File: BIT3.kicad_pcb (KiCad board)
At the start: 2 copper layers, 121.3 x 109.4 mm, 49 parts, among them J1 Conn_02x04_Odd_Even, J2 Conn_01x02_Pin, J3 Conn_01x04_Socket, J4 Conn_02x02_Odd_Even, Q1 2SC1815, SW1 SW_SPDT, SW2 SW_Push, SW3 SW_Push, U2 FODM217A, U3 FODM217A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

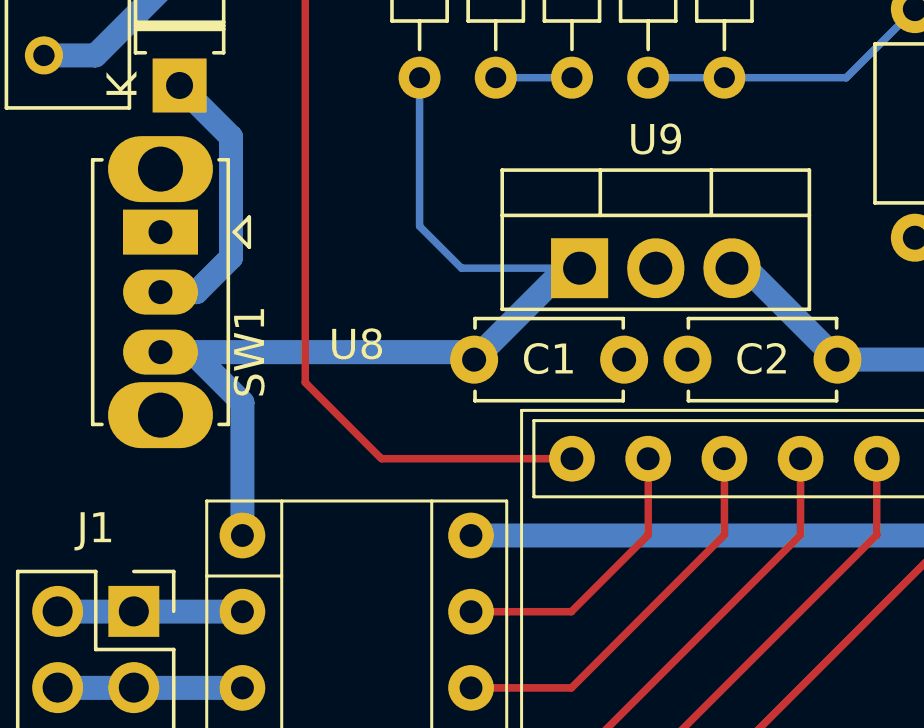
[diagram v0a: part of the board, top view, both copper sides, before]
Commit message: モータの電源を BATT から 5V に変更
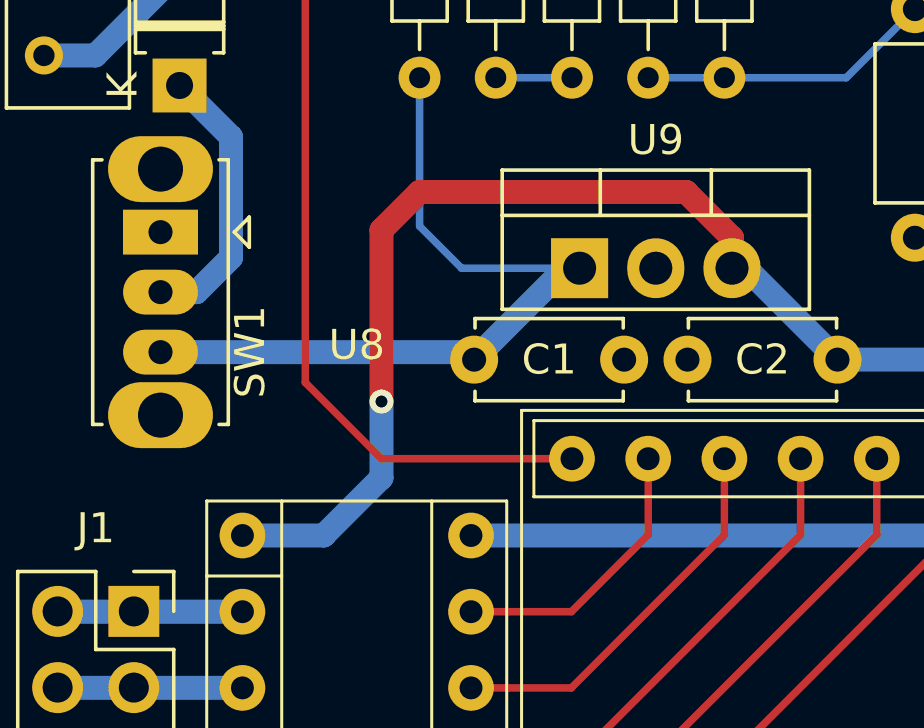
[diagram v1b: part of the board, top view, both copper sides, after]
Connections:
- U8 pad 1: /V_Battery -> +5V
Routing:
- net +5V: track 52.9 -> 80.5 mm, vias 3 -> 4
- net /V_Battery: track 34.1 -> 27.2 mm
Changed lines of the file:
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@@
       (stroke (width 0.1) (type default)) (layer "F.SilkS"))
     (pad "1" thru_hole circle (at -3.81 -6.35) (size 1.524 1.524) (drill 0.762) (layers "*.Cu" "*.Mask")
-      (net 64 "/V_Battery") (pinfunction "VM") (pintype "power_in"))
+      (net 14 "+5V") (pinfunction "VM") (pintype "power_in"))
     (pad "2" thru_hole circle (at -3.81 -3.81) (size 1.524 1.524) (drill 0.762) (layers "*.Cu" "*.Mask")
       (net 37 "Net-(J1-Pin_1)") (pinfunction "AOUT1") (pintype "output"))
@@
   (segment (start 190.5 76.835) (end 220.5 76.835) (width 0.25) (layer "F.Cu") (net 13))
   (segment (start 161.29 78.486) (end 161.29 80.264) (width 0.25) (layer "F.Cu") (net 13))
+  (segment (start 125.73 87.63) (end 125.73 93.345) (width 0.8) (layer "F.Cu") (net 14))
+  (segment (start 127 86.36) (end 125.73 87.63) (width 0.8) (layer "F.Cu") (net 14))
   (segment (start 171.704 91.948) (end 172.72 92.964) (width 0.8) (layer "F.Cu") (net 14))
   (segment (start 158.496 91.948) (end 171.704 91.948) (width 0.8) (layer "F.Cu") (net 14))
+  (segment (start 137.414 87.884) (end 135.89 86.36) (width 0.8) (layer "F.Cu") (net 14))
+  (segment (start 135.89 86.36) (end 127 86.36) (width 0.8) (layer "F.Cu") (net 14))
+  (segment (start 137.414 88.9) (end 137.414 87.884) (width 0.8) (layer "F.Cu") (net 14))
   (segment (start 172.72 92.964) (end 172.72 95.25) (width 0.8) (layer "F.Cu") (net 14))
   (via (at 160.02 91.948) (size 0.8) (drill 0.4) (layers "F.Cu" "B.Cu") (net 14))
   (via (at 158.496 91.948) (size 0.8) (drill 0.4) (layers "F.Cu" "B.Cu") (net 14))
   (via (at 159.258 91.948) (size 0.8) (drill 0.4) (layers "F.Cu" "B.Cu") (net 14))
+  (via (at 125.73 93.345) (size 0.8) (drill 0.4) (layers "F.Cu" "B.Cu") (net 14))
+  (segment (start 123.805 97.81) (end 121.095 97.81) (width 0.8) (layer "B.Cu") (net 14))
   (segment (start 177.165 97.155) (end 177.165 100.33) (width 0.8) (layer "B.Cu") (net 14))
   (segment (start 158.496 91.948) (end 159.258 91.948) (width 0.8) (layer "B.Cu") (net 14))
@@
   (segment (start 140.93 91.948) (end 158.496 91.948) (width 0.8) (layer "B.Cu") (net 14))
   (segment (start 177.165 100.33) (end 178.435 101.6) (width 0.8) (layer "B.Cu") (net 14))
+  (segment (start 125.73 93.345) (end 125.73 95.885) (width 0.8) (layer "B.Cu") (net 14))
+  (segment (start 125.73 95.885) (end 123.805 97.81) (width 0.8) (layer "B.Cu") (net 14))
   (segment (start 159.258 91.948) (end 160.02 91.948) (width 0.8) (layer "B.Cu") (net 14))
   (segment (start 191.77 58.27) (end 188.5 55) (width 0.25) (layer "F.Cu") (net 15))
@@
   (segment (start 119.414 91.698) (end 118.364 91.698) (width 0.8) (layer "B.Cu") (net 64))
   (segment (start 131.866 88.9) (end 128.818 91.948) (width 0.8) (layer "B.Cu") (net 64))
-  (segment (start 121.095 93.379) (end 119.414 91.698) (width 0.8) (layer "B.Cu") (net 64))
   (segment (start 128.568 91.698) (end 128.818 91.948) (width 0.8) (layer "B.Cu") (net 64))
-  (segment (start 121.095 97.81) (end 121.095 93.379) (width 0.8) (layer "B.Cu") (net 64))
   (segment (start 165.1 106.68) (end 180.34 106.68) (width 0.25) (layer "B.Cu") (net 65))
   (segment (start 151.13 104.14) (end 144.78 110.49) (width 0.25) (layer "B.Cu") (net 66))

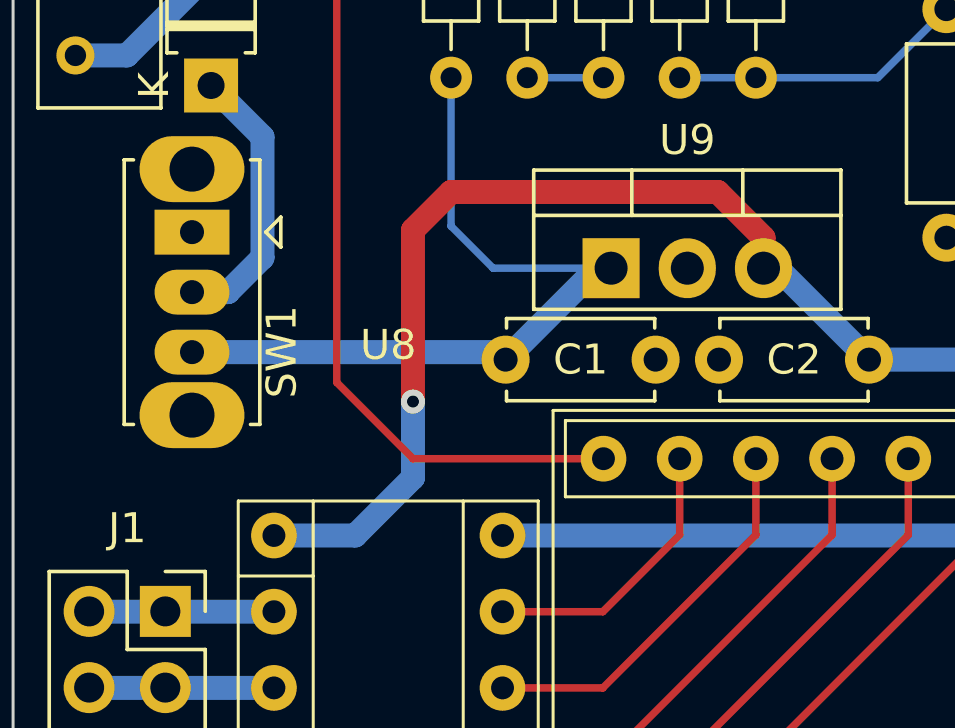
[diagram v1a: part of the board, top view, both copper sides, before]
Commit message: モータ電源を BATT に戻した
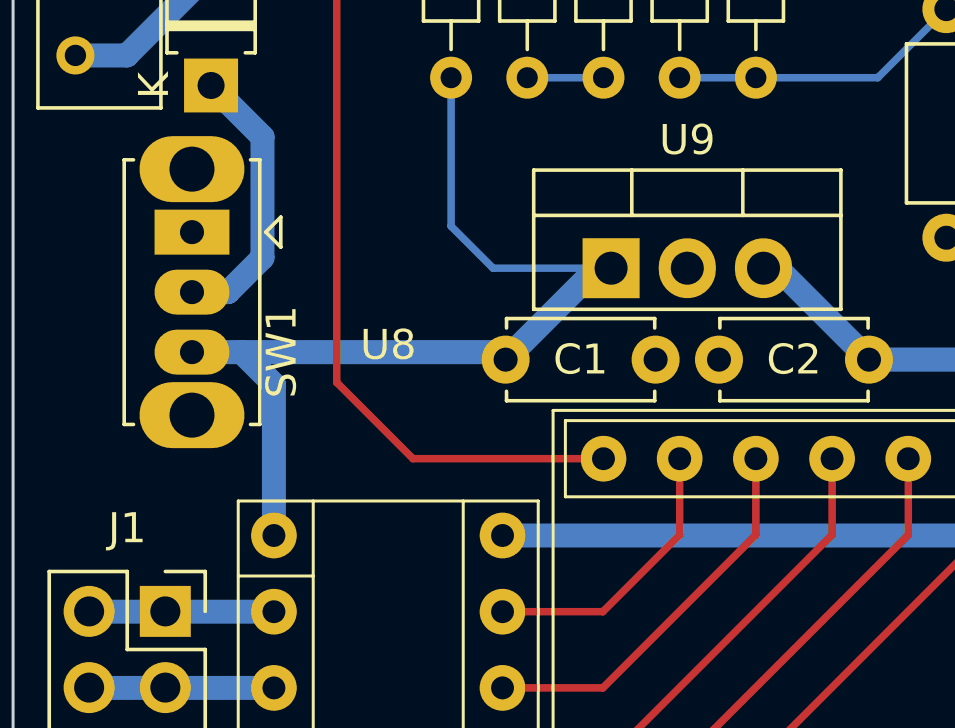
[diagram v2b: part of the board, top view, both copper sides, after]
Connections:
- U8 pad 1: +5V -> /V_Battery
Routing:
- net +5V: track 80.5 -> 52.9 mm, vias 4 -> 3
- net /V_Battery: track 27.2 -> 32.8 mm
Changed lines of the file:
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@@
       (stroke (width 0.1) (type default)) (layer "F.SilkS"))
     (pad "1" thru_hole circle (at -3.81 -6.35) (size 1.524 1.524) (drill 0.762) (layers "*.Cu" "*.Mask")
-      (net 14 "+5V") (pinfunction "VM") (pintype "power_in"))
+      (net 64 "/V_Battery") (pinfunction "VM") (pintype "power_in"))
     (pad "2" thru_hole circle (at -3.81 -3.81) (size 1.524 1.524) (drill 0.762) (layers "*.Cu" "*.Mask")
       (net 37 "Net-(J1-Pin_1)") (pinfunction "AOUT1") (pintype "output"))
@@
   (segment (start 190.5 76.835) (end 220.5 76.835) (width 0.25) (layer "F.Cu") (net 13))
   (segment (start 161.29 78.486) (end 161.29 80.264) (width 0.25) (layer "F.Cu") (net 13))
-  (segment (start 125.73 87.63) (end 125.73 93.345) (width 0.8) (layer "F.Cu") (net 14))
-  (segment (start 127 86.36) (end 125.73 87.63) (width 0.8) (layer "F.Cu") (net 14))
   (segment (start 171.704 91.948) (end 172.72 92.964) (width 0.8) (layer "F.Cu") (net 14))
   (segment (start 158.496 91.948) (end 171.704 91.948) (width 0.8) (layer "F.Cu") (net 14))
-  (segment (start 137.414 87.884) (end 135.89 86.36) (width 0.8) (layer "F.Cu") (net 14))
-  (segment (start 135.89 86.36) (end 127 86.36) (width 0.8) (layer "F.Cu") (net 14))
-  (segment (start 137.414 88.9) (end 137.414 87.884) (width 0.8) (layer "F.Cu") (net 14))
   (segment (start 172.72 92.964) (end 172.72 95.25) (width 0.8) (layer "F.Cu") (net 14))
   (via (at 160.02 91.948) (size 0.8) (drill 0.4) (layers "F.Cu" "B.Cu") (net 14))
   (via (at 158.496 91.948) (size 0.8) (drill 0.4) (layers "F.Cu" "B.Cu") (net 14))
   (via (at 159.258 91.948) (size 0.8) (drill 0.4) (layers "F.Cu" "B.Cu") (net 14))
-  (via (at 125.73 93.345) (size 0.8) (drill 0.4) (layers "F.Cu" "B.Cu") (net 14))
-  (segment (start 123.805 97.81) (end 121.095 97.81) (width 0.8) (layer "B.Cu") (net 14))
   (segment (start 177.165 97.155) (end 177.165 100.33) (width 0.8) (layer "B.Cu") (net 14))
   (segment (start 158.496 91.948) (end 159.258 91.948) (width 0.8) (layer "B.Cu") (net 14))
@@
   (segment (start 140.93 91.948) (end 158.496 91.948) (width 0.8) (layer "B.Cu") (net 14))
   (segment (start 177.165 100.33) (end 178.435 101.6) (width 0.8) (layer "B.Cu") (net 14))
-  (segment (start 125.73 93.345) (end 125.73 95.885) (width 0.8) (layer "B.Cu") (net 14))
-  (segment (start 125.73 95.885) (end 123.805 97.81) (width 0.8) (layer "B.Cu") (net 14))
   (segment (start 159.258 91.948) (end 160.02 91.948) (width 0.8) (layer "B.Cu") (net 14))
   (segment (start 191.77 58.27) (end 188.5 55) (width 0.25) (layer "F.Cu") (net 15))
@@
   (segment (start 127 87.5) (end 128.4 88.9) (width 0.25) (layer "B.Cu") (net 64))
   (segment (start 132.334 88.9) (end 131.866 88.9) (width 0.8) (layer "B.Cu") (net 64))
+  (segment (start 120.015 91.698) (end 128.568 91.698) (width 0.8) (layer "B.Cu") (net 64))
   (segment (start 127 82.55) (end 127 87.5) (width 0.25) (layer "B.Cu") (net 64))
-  (segment (start 118.364 91.698) (end 128.568 91.698) (width 0.8) (layer "B.Cu") (net 64))
   (segment (start 128.4 88.9) (end 132.334 88.9) (width 0.25) (layer "B.Cu") (net 64))
-  (segment (start 119.414 91.698) (end 118.364 91.698) (width 0.8) (layer "B.Cu") (net 64))
+  (segment (start 118.364 91.698) (end 120.015 91.698) (width 0.8) (layer "B.Cu") (net 64))
+  (segment (start 120.015 91.698) (end 121.095 92.778) (width 0.8) (layer "B.Cu") (net 64))
   (segment (start 131.866 88.9) (end 128.818 91.948) (width 0.8) (layer "B.Cu") (net 64))
+  (segment (start 121.095 92.778) (end 121.095 97.81) (width 0.8) (layer "B.Cu") (net 64))
   (segment (start 128.568 91.698) (end 128.818 91.948) (width 0.8) (layer "B.Cu") (net 64))
   (segment (start 165.1 106.68) (end 180.34 106.68) (width 0.25) (layer "B.Cu") (net 65))

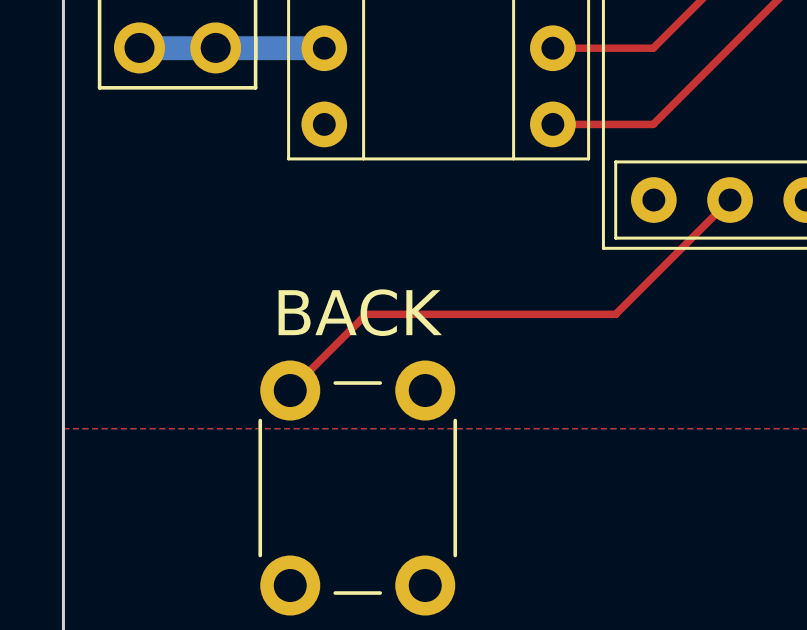
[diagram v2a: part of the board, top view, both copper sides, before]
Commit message: BACK -> EXEC
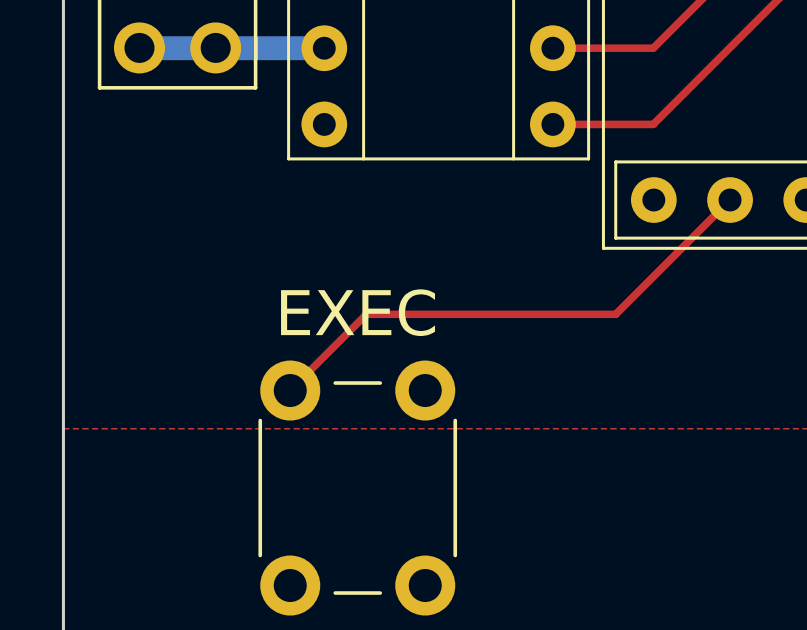
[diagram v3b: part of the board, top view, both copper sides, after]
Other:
- board text added: "EXEC"
- board text removed: "BACK"
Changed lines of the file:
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@@
     )
   )
-  (gr_text "BACK" (at 122.174 116.84) (layer "F.SilkS")
+  (gr_text "EXEC" (at 122.174 116.84) (layer "F.SilkS")
     (effects (font (size 1.5 1.5) (thickness 0.2)))
   )

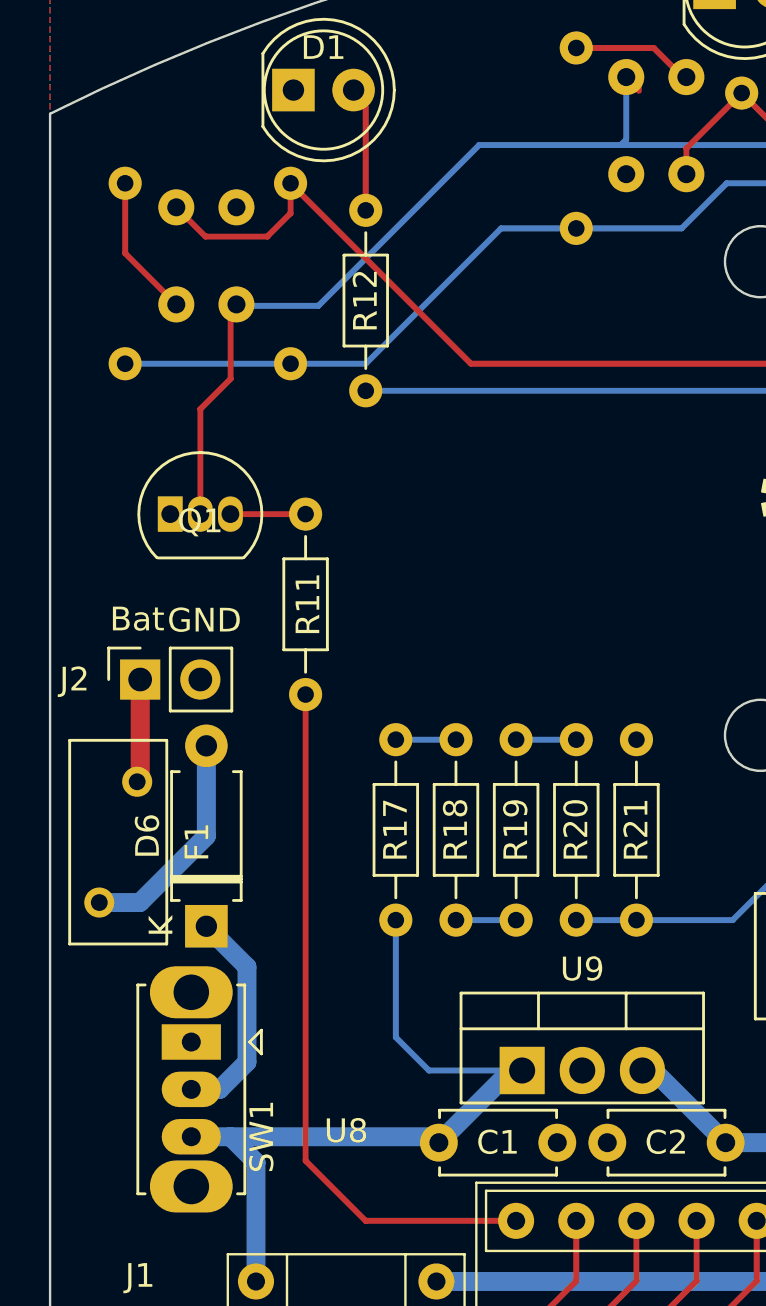
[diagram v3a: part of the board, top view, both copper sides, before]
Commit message: 赤外線 LED 用トランジスタを変更
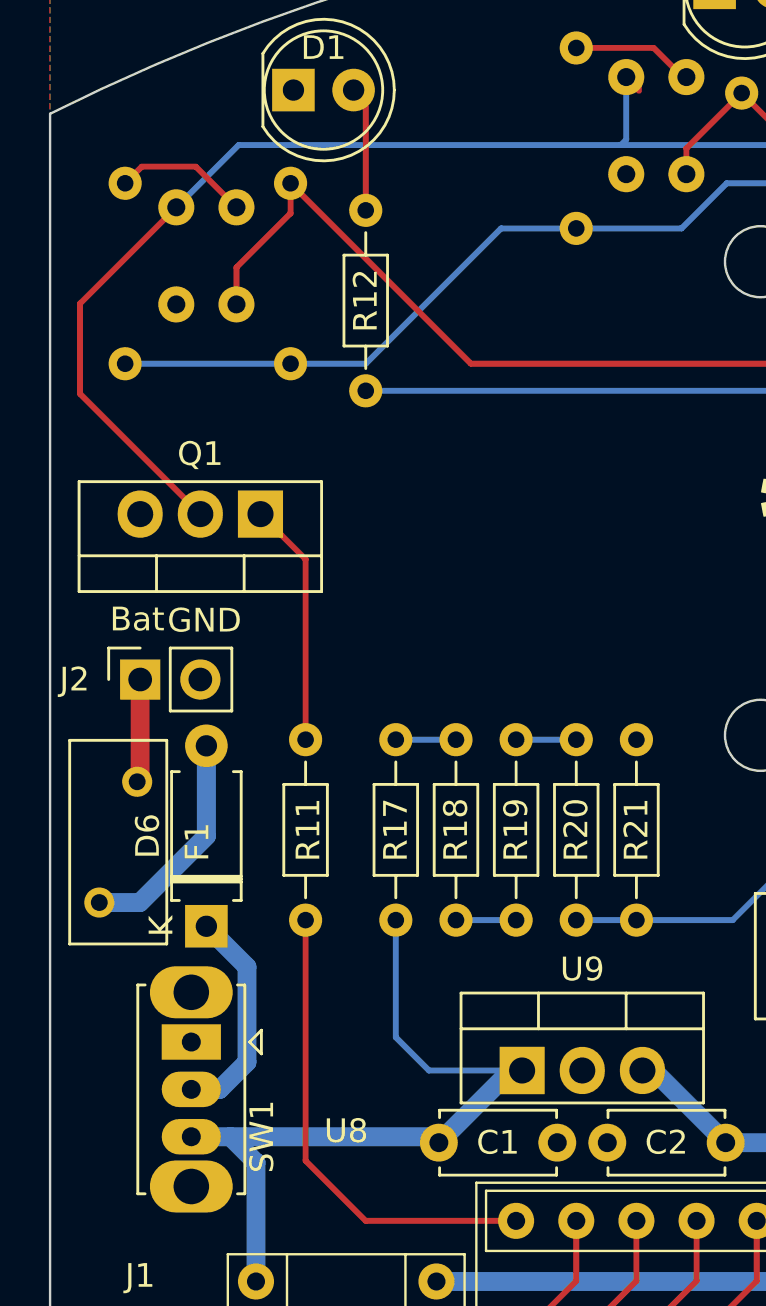
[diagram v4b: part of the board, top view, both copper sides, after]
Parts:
- Q1: value 2SC1815 -> BSP89; footprint Package_TO_SOT_THT:TO-92_Inline -> Package_TO_SOT_THT:TO-220-3_Vertical
- moved R11 9.52 mm to (123.2, 82.5)
- moved Q1 3.81 mm to (121.3, 65.4), turned to 180 degrees
- turned U2 to 180 degrees
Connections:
- Q1 pad 1: GND -> Net-(Q1-G)
- Q1 pad 3: Net-(Q1-B) -> GND
- R11 pad 2: Net-(Q1-B) -> Net-(Q1-G)
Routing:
- net Net-(Q1-G): track 0.00 -> 10.3 mm
- net /FET_B: track 29.6 -> 20.1 mm
- net /FET_D: track 145.7 -> 153.6 mm
- net Net-(Q1-B): track 3.17 -> 0.00 mm
- net /sensor_L: track 56.2 -> 55.6 mm

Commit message: Tr 置き換え，部品表更新
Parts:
- moved R11 5.72 mm to (123.2, 76.8)
- moved Q1 1.91 mm to (121.3, 63.5)
- turned U2 to 0 degrees
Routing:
- net /FET_D: track 153.6 -> 143.8 mm
- net /FET_B: track 20.1 -> 25.8 mm
- net Net-(Q1-G): track 10.3 -> 6.50 mm
- net /sensor_L: track 55.6 -> 56.2 mm
